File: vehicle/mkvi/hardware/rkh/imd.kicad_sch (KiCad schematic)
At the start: 4 parts, among them J1301 Automotive_M.2, K1201 G6L-1P_DC5, Q1201 SSM3K333R, SW1201 SW_SPST

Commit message: m.2 connectors
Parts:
- J1301: symbol formula:Automotive_M.2 -> OEM:Automotive_M.2
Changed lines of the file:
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@@
     (pin "1")
   )
-  (symbol (lib_id "formula:Automotive_M.2") (at 148.59 81.28 0) (unit 1)
+  (symbol (lib_id "OEM:Automotive_M.2") (at 148.59 81.28 0) (unit 1)
     (in_bom yes) (on_board yes) (fields_autoplaced)
     (property "Reference" "J1301" (id 0) (at 148.59 31.75 0)

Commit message: nmos
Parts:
- Q1201: symbol formula:SSM3K333R -> OEM:SSM3K333R
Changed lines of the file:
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@@
     (pin "8")
   )
-  (symbol (lib_id "formula:SSM3K333R") (at 57.15 69.85 0) (unit 1)
+  (symbol (lib_id "OEM:SSM3K333R") (at 57.15 69.85 0) (unit 1)
     (in_bom yes) (on_board yes)
     (property "Reference" "Q1201" (id 0) (at 54.61 63.5 0)

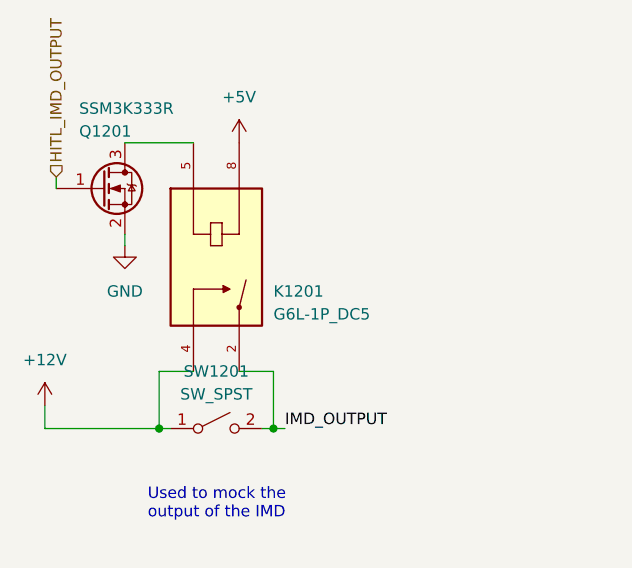
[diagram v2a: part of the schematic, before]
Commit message: update boards from library, fix issues that arose
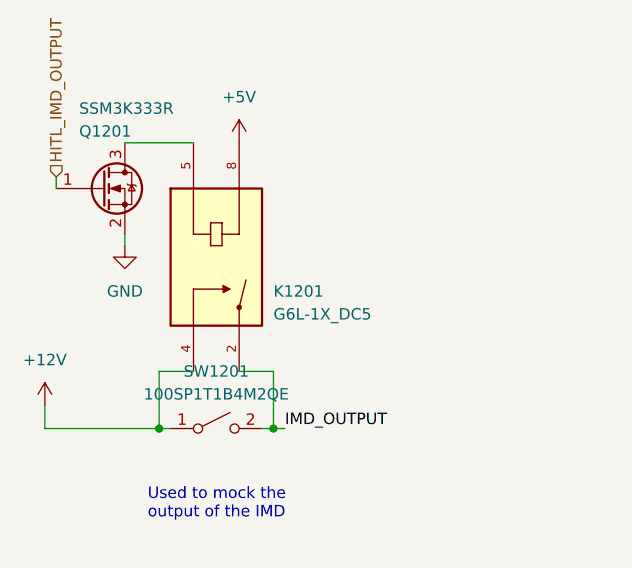
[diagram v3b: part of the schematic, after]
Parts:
- J1301: DKPN (none) -> MOUSER:945-CNU027S0672001VE; MFN (none) -> Yamaichi Electronics; MPN (none) -> CNU027S-067-2001-VE; NewDesigns (none) -> YES; Package (none) -> Custom; Stocked (none) -> Tape; Style (none) -> SMD
- K1201: value G6L-1P_DC5 -> G6L-1X_DC5; symbol formula:G6L-1P_DC5 -> OEM:G6L-1X_DC5; AVAILABILITY Unavailable -> (none); DESCRIPTION Telecom Relay SPST-NO (1 Form A) Through Hole -> (none); DKPN (none) -> Z1228-ND; MF Omron Electronics -> (none); MFN (none) -> Omron Electronics; MP G6L-1P-DC24 -> (none); MPN G6L-1P-DC24 -> G6L-1P DC5; Manufacturer Omron Electronics -> (none); NewDesigns (none) -> YES; PACKAGE None -> (none); PRICE None -> (none); Package (none) -> Custom; Stocked (none) -> Tube; Style (none) -> THT
- Q1201: footprint footprints:SOT-23F -> OEM:SOT-23F; DKPN (none) -> SSM3K333RLFDKR-ND; MFN DK -> Toshiba; MPN SSM3K333RLFCT-ND -> SSM3K333R,LF; NewDesigns (none) -> YES; Package (none) -> SOT-23; PurchasingLink https://www.digikey.com/product-detail/en/toshiba-semicondu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 -> (none); Stocked (none) -> Digi-Reel; Style (none) -> SMD
- SW1201: value SW_SPST -> 100SP1T1B4M2QE; symbol Switch:SW_SPST -> OEM:100SP1T1B4M2QE; DKPN (none) -> EG2355-ND; MFN (none) -> E-Switch; MPN (none) -> 100SP1T1B4M2QE; NewDesigns (none) -> YES; Package (none) -> Custom; Stocked (none) -> Bulk; Style (none) -> THT
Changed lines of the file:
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@@
     (effects (font (size 1.27 1.27)) (justify right))
   )
-  (symbol (lib_name "+5V_1") (lib_id "power:+5V") (at 121.92 139.7 0) (unit 1)
+  (symbol (lib_id "power:+5V") (at 121.92 139.7 0) (unit 1)
     (in_bom yes) (on_board yes) (fields_autoplaced)
     (property "Reference" "#PWR?" (id 0) (at 121.92 143.51 0)
@@
       (effects (font (size 1.27 1.27)) hide)
     )
-    (property "Datasheet" "" (id 3) (at 140.97 127 0)
+    (property "Datasheet" "https://www.mouser.com/catalog/specsheets/Yamaichi_04142021_CNU027S-067-2001-VE_DataSheet_Ver_A.pdf" (id 3) (at 140.97 127 0)
+      (effects (font (size 1.27 1.27)) hide)
+    )
+    (property "MPN" "CNU027S-067-2001-VE" (id 4) (at 148.59 81.28 0)
+      (effects (font (size 1.27 1.27)) hide)
+    )
+    (property "MFN" "Yamaichi Electronics" (id 5) (at 148.59 81.28 0)
+      (effects (font (size 1.27 1.27)) hide)
+    )
+    (property "DKPN" "MOUSER:945-CNU027S0672001VE" (id 6) (at 148.59 81.28 0)
+      (effects (font (size 1.27 1.27)) hide)
+    )
+    (property "NewDesigns" "YES" (id 7) (at 148.59 81.28 0)
+      (effects (font (size 1.27 1.27)) hide)
+    )
+    (property "Stocked" "Tape" (id 8) (at 148.59 81.28 0)
+      (effects (font (size 1.27 1.27)) hide)
+    )
+    (property "Package" "Custom" (id 9) (at 148.59 81.28 0)
+      (effects (font (size 1.27 1.27)) hide)
+    )
+    (property "Style" "SMD" (id 10) (at 148.59 81.28 0)
       (effects (font (size 1.27 1.27)) hide)
     )
@@
     (pin "1")
   )
-  (symbol (lib_id "power:+12V") (at 115.57 43.18 0) (unit 1)
+  (symbol (lib_name "+12V_1") (lib_id "power:+12V") (at 115.57 43.18 0) (unit 1)
     (in_bom yes) (on_board yes) (fields_autoplaced)
     (property "Reference" "#PWR?" (id 0) (at 115.57 46.99 0)
@@
     (pin "1")
   )
-  (symbol (lib_id "Switch:SW_SPST") (at 69.85 96.52 0) (unit 1)
+  (symbol (lib_id "OEM:100SP1T1B4M2QE") (at 69.85 96.52 0) (unit 1)
     (in_bom yes) (on_board yes) (fields_autoplaced)
     (property "Reference" "SW1201" (id 0) (at 69.85 90.17 0))
-    (property "Value" "SW_SPST" (id 1) (at 69.85 92.71 0))
+    (property "Value" "100SP1T1B4M2QE" (id 1) (at 69.85 92.71 0))
     (property "Footprint" "footprints:SW_100SP1T1B4M2QE" (id 2) (at 69.85 96.52 0)
       (effects (font (size 1.27 1.27)) hide)
     )
-    (property "Datasheet" "~" (id 3) (at 69.85 96.52 0)
+    (property "Datasheet" "https://sten-eswitch-13110800-production.s3.amazonaws.com/system/asset/product_line/data_sheet/129/100.pdf" (id 3) (at 69.85 96.52 0)
+      (effects (font (size 1.27 1.27)) hide)
+    )
+    (property "MPN" "100SP1T1B4M2QE" (id 4) (at 69.85 96.52 0)
+      (effects (font (size 1.27 1.27)) hide)
+    )
+    (property "MFN" "E-Switch" (id 5) (at 69.85 96.52 0)
+      (effects (font (size 1.27 1.27)) hide)
+    )
+    (property "DKPN" "EG2355-ND" (id 6) (at 69.85 96.52 0)
+      (effects (font (size 1.27 1.27)) hide)
+    )
+    (property "NewDesigns" "YES" (id 7) (at 69.85 96.52 0)
+      (effects (font (size 1.27 1.27)) hide)
+    )
+    (property "Stocked" "Bulk" (id 8) (at 69.85 96.52 0)
+      (effects (font (size 1.27 1.27)) hide)
+    )
+    (property "Package" "Custom" (id 9) (at 69.85 96.52 0)
+      (effects (font (size 1.27 1.27)) hide)
+    )
+    (property "Style" "THT" (id 10) (at 69.85 96.52 0)
       (effects (font (size 1.27 1.27)) hide)
     )
@@
     (pin "2")
   )
-  (symbol (lib_name "G6L-1P_DC5_2") (lib_id "formula:G6L-1P_DC5") (at 69.85 77.47 270) (unit 1)
+  (symbol (lib_id "OEM:G6L-1X_DC5") (at 69.85 77.47 270) (unit 1)
     (in_bom yes) (on_board yes)
     (property "Reference" "K1201" (id 0) (at 76.2 81.28 90)
       (effects (font (size 1.27 1.27)) (justify left))
     )
-    (property "Value" "G6L-1P_DC5" (id 1) (at 76.2 83.82 90)
+    (property "Value" "G6L-1X_DC5" (id 1) (at 76.2 83.82 90)
       (effects (font (size 1.27 1.27)) (justify left))
     )
@@
       (effects (font (size 1.27 1.27)) hide)
     )
-    (property "PRICE" "None" (id 4) (at 69.85 77.47 0)
+    (property "MPN" "G6L-1P DC5" (id 10) (at 69.85 77.47 0)
       (effects (font (size 1.27 1.27)) (justify bottom) hide)
     )
-    (property "MP" "G6L-1P-DC24" (id 5) (at 69.85 77.47 0)
+    (property "MFN" "Omron Electronics" (id 5) (at 83.82 77.47 0)
       (effects (font (size 1.27 1.27)) (justify bottom) hide)
     )
-    (property "PACKAGE" "None" (id 6) (at 69.85 77.47 0)
-      (effects (font (size 1.27 1.27)) (justify bottom) hide)
-    )
-    (property "AVAILABILITY" "Unavailable" (id 7) (at 69.85 77.47 0)
-      (effects (font (size 1.27 1.27)) (justify bottom) hide)
-    )
-    (property "DESCRIPTION" "Telecom Relay SPST-NO (1 Form A) Through Hole" (id 8) (at 80.01 77.47 0)
-      (effects (font (size 1.27 1.27)) (justify bottom) hide)
-    )
-    (property "MF" "Omron Electronics" (id 9) (at 83.82 77.47 0)
-      (effects (font (size 1.27 1.27)) (justify bottom) hide)
-    )
-    (property "MPN" "G6L-1P-DC24" (id 10) (at 69.85 77.47 0)
-      (effects (font (size 1.27 1.27)) (justify bottom) hide)
-    )
-    (property "Manufacturer" "Omron Electronics" (id 11) (at 83.82 77.47 0)
-      (effects (font (size 1.27 1.27)) (justify bottom) hide)
+    (property "DKPN" "Z1228-ND" (id 6) (at 69.85 77.47 0)
+      (effects (font (size 1.27 1.27)) hide)
+    )
+    (property "NewDesigns" "YES" (id 7) (at 69.85 77.47 0)
+      (effects (font (size 1.27 1.27)) hide)
+    )
+    (property "Stocked" "Tube" (id 8) (at 69.85 77.47 0)
+      (effects (font (size 1.27 1.27)) hide)
+    )
+    (property "Package" "Custom" (id 9) (at 69.85 77.47 0)
+      (effects (font (size 1.27 1.27)) hide)
+    )
+    (property "Style" "THT" (id 11) (at 69.85 77.47 0)
+      (effects (font (size 1.27 1.27)) hide)
     )
     (pin "2")
@@
       (effects (font (size 1.27 1.27)) (justify left))
     )
-    (property "Footprint" "footprints:SOT-23F" (id 2) (at 62.23 71.755 0)
+    (property "Footprint" "OEM:SOT-23F" (id 2) (at 62.23 71.755 0)
       (effects (font (size 1.27 1.27) italic) (justify left) hide)
     )
-    (property "Datasheet" "https://drive.google.com/drive/folders/0B-V-iZf33Y4GNzhDQTJZanJRbVk" (id 3) (at 62.23 67.945 0)
+    (property "Datasheet" "${OEM_DIR}/parts/datasheets/toshiba_SSM3K333R.pdf" (id 3) (at 62.23 67.945 0)
       (effects (font (size 1.27 1.27)) (justify left) hide)
     )
-    (property "MFN" "DK" (id 4) (at 69.85 60.325 0)
+    (property "MFN" "Toshiba" (id 4) (at 69.85 60.325 0)
       (effects (font (size 1.524 1.524)) hide)
     )
-    (property "MPN" "SSM3K333RLFCT-ND" (id 5) (at 67.31 62.865 0)
+    (property "MPN" "SSM3K333R,LF" (id 5) (at 67.31 62.865 0)
       (effects (font (size 1.524 1.524)) hide)
     )
-    (property "PurchasingLink" "https://www.digikey.com/product-detail/en/toshiba-semiconductor-and-storage/SSM3K333RLF/SSM3K333RLFCT-ND/3522391" (id 6) (at 64.77 65.405 0)
-      (effects (font (size 1.524 1.524)) hide)
-    )
-    (pin "1")
+    (property "DKPN" "SSM3K333RLFDKR-ND" (id 6) (at 57.15 69.85 0)
+      (effects (font (size 1.27 1.27)) hide)
+    )
+    (property "Package" "SOT-23" (id 7) (at 57.15 69.85 0)
+      (effects (font (size 1.27 1.27)) hide)
+    )
+    (property "NewDesigns" "YES" (id 8) (at 57.15 69.85 0)
+      (effects (font (size 1.27 1.27)) hide)
+    )
+    (property "Stocked" "Digi-Reel" (id 9) (at 57.15 69.85 0)
+      (effects (font (size 1.27 1.27)) hide)
+    )
+    (property "Style" "SMD" (id 10) (at 57.15 69.85 0)
+      (effects (font (size 1.27 1.27)) hide)
+    )
+    (pin "1")

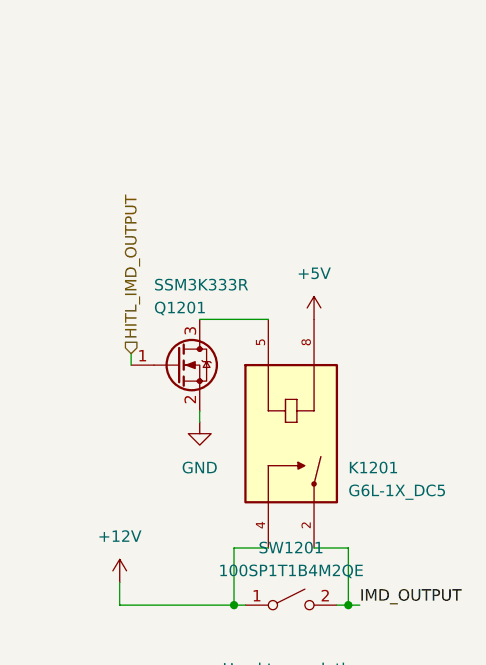
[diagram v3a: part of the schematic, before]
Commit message: Add pull-down resistors on FET gates
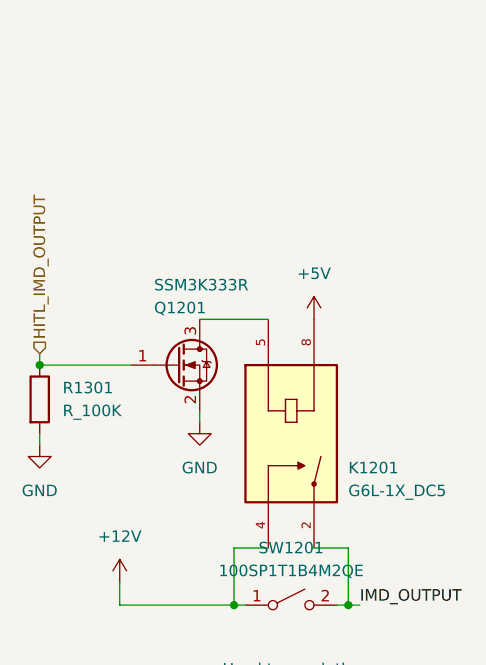
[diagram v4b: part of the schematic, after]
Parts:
- added R1301: R_100K, OEM:R_0603, symbol formula:R_100K
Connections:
- net GND: now also R1301.2
- net HITL_IMD_OUTPUT: now also R1301.1
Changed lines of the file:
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@@
 (kicad_sch (version 20211123) (generator eeschema)
   (paper "A4")
+  (junction (at 41.91 69.85) (diameter 0) (color 0 0 0 0)
+  )
   (junction (at 135.89 41.91) (diameter 0) (color 0 0 0 0)
   )
@@
     (stroke (width 0) (type default) (color 0 0 0 0))
   )
-  (wire (pts (xy 52.07 68.58) (xy 52.07 69.85))
-    (stroke (width 0) (type default) (color 0 0 0 0))
-  )
   (wire (pts (xy 76.2 90.17) (xy 76.2 96.52))
     (stroke (width 0) (type default) (color 0 0 0 0))
   )
+  (wire (pts (xy 41.91 69.85) (xy 52.07 69.85))
+    (stroke (width 0) (type default) (color 0 0 0 0))
+  )
+  (wire (pts (xy 41.91 68.58) (xy 41.91 69.85))
+    (stroke (width 0) (type default) (color 0 0 0 0))
+  )
   (wire (pts (xy 63.5 90.17) (xy 63.5 96.52))
     (stroke (width 0) (type default) (color 0 0 0 0))
@@
   )
   (wire (pts (xy 135.89 41.91) (xy 135.89 43.18))
+    (stroke (width 0) (type default) (color 0 0 0 0))
+  )
+  (wire (pts (xy 41.91 77.47) (xy 41.91 78.74))
     (stroke (width 0) (type default) (color 0 0 0 0))
   )
@@
     (effects (font (size 1.27 1.27)) (justify right))
   )
-  (hierarchical_label "HITL_IMD_OUTPUT" (shape input) (at 52.07 68.58 90)
+  (hierarchical_label "HITL_IMD_OUTPUT" (shape input) (at 41.91 68.58 90)
     (effects (font (size 1.27 1.27)) (justify left))
   )
@@
     (effects (font (size 1.27 1.27)) (justify right))
   )
+  (symbol (lib_id "power:GND") (at 41.91 78.74 0) (unit 1)
+    (in_bom yes) (on_board yes) (fields_autoplaced)
+    (property "Reference" "#PWR?" (id 0) (at 41.91 85.09 0)
+      (effects (font (size 1.27 1.27)) hide)
+    )
+    (property "Value" "GND" (id 1) (at 41.91 83.82 0))
+    (property "Footprint" "" (id 2) (at 41.91 78.74 0)
+      (effects (font (size 1.27 1.27)) hide)
+    )
+    (property "Datasheet" "" (id 3) (at 41.91 78.74 0)
+      (effects (font (size 1.27 1.27)) hide)
+    )
+    (pin "1")
+  )
+  (symbol (lib_id "formula:R_100K") (at 41.91 73.66 0) (unit 1)
+    (in_bom yes) (on_board yes) (fields_autoplaced)
+    (property "Reference" "R1301" (id 0) (at 44.45 72.3899 0)
+      (effects (font (size 1.27 1.27)) (justify left))
+    )
+    (property "Value" "R_100K" (id 1) (at 44.45 74.9299 0)
+      (effects (font (size 1.27 1.27)) (justify left))
+    )
+    (property "Footprint" "OEM:R_0603" (id 2) (at 40.132 73.66 0)
+      (effects (font (size 1.27 1.27)) hide)
+    )
+    (property "Datasheet" "https://industrial.panasonic.com/cdbs/www-data/pdf/RDA0000/AOA0000C304.pdf" (id 3) (at 43.942 73.66 0)
+      (effects (font (size 1.27 1.27)) hide)
+    )
+    (property "MFN" "DK" (id 4) (at 41.91 73.66 0)
+      (effects (font (size 1.524 1.524)) hide)
+    )
+    (property "MPN" "P100KCCT-ND" (id 5) (at 41.91 73.66 0)
+      (effects (font (size 1.524 1.524)) hide)
+    )
+    (property "PurchasingLink" "https://www.digikey.com/product-detail/en/panasonic-electronic-components/ERJ-6ENF1003V/P100KCCT-ND/119551" (id 6) (at 54.102 63.5 0)
+      (effects (font (size 1.524 1.524)) hide)
+    )
+    (pin "1")
+    (pin "2")
+  )
   (symbol (lib_id "power:+5V") (at 121.92 139.7 0) (unit 1)
